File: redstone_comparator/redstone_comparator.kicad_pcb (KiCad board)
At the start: 2 copper layers, 40 x 40 mm, 77 parts, among them J1 1x4_Pogo, J2 1x4_Pogo, J3 1x4_Pogo, J4 1x4_Pogo, J5 1x4_Pogo, J6 1x4_Pogo, J7 1x4_Pogo, J8 1x4_Pogo, J9 2.54mm_ProgrammingPin, Q1 MMBT3904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

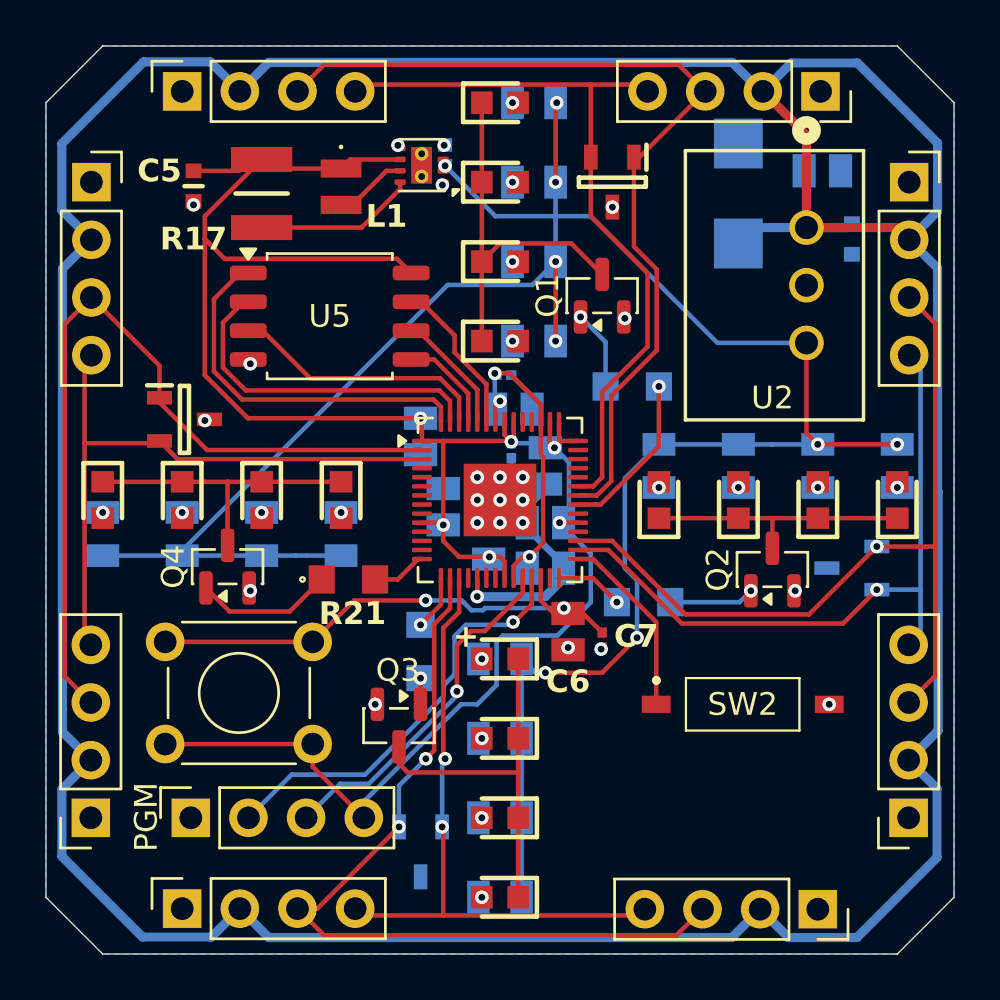
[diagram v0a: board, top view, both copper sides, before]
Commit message: finish routing all connections, todo align components and make it symmetric
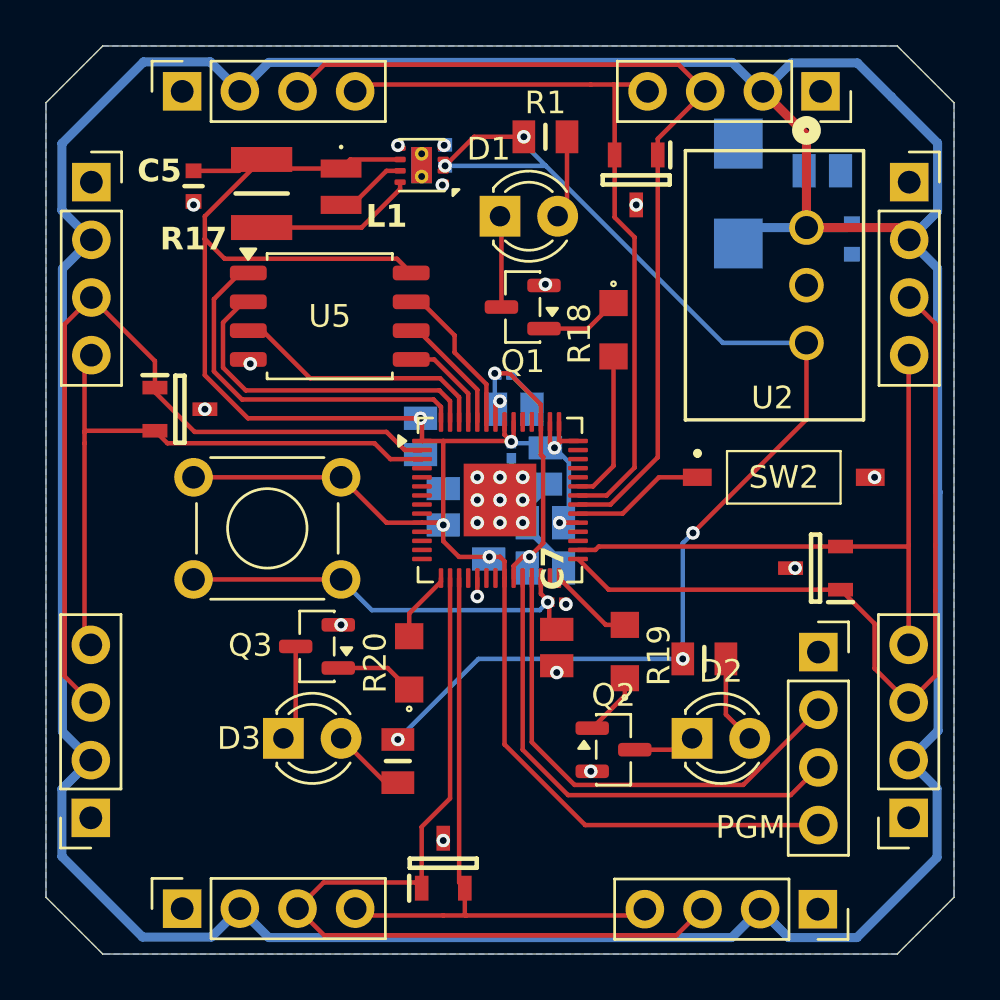
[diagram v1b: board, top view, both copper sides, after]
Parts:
- removed D10, D11, D12, D13, D14, D15, D16, D4, D5, D6, D7, D8, D9: LED, SamacSys_Parts:LEDC1608X115N
- removed Q4: MMBT3904, Package_TO_SOT_SMD:SOT-23
- removed R10, R11, R12, R13, R14, R15, R16, R4, R5, R6, R7, R8, R9: 200, SamacSys_Parts:CRCW1210200RJNEAIF
- removed R21: 1k, SamacSys_Parts:ERJ-UP6D1001V
- D1, D2, D3: footprint SamacSys_Parts:LEDC1608X115N -> LED_THT:LED_D3.0mm
- D18, D20, R1, R18, R19, R2, R20, R3: moved to F.Cu
- moved J9 28.6 mm to (149.0, 61.7), turned to 0 degrees
- moved D2 25.9 mm to (143.5, 65.5)
- moved D3 23.1 mm to (125.5, 65.5)
- moved R3 22.8 mm to (130.5, 66.5), turned to -90 degrees
- moved R2 22.3 mm to (144.0, 62.0), turned to 0 degrees
- moved SW1 12.9 mm to (121.5, 54.0), turned to 0 degrees
- moved Q2 10.6 mm to (140.0, 66.0), turned to 0 degrees
- moved SW2 10.2 mm to (147.5, 54.0)
- moved Q3 5.02 mm to (126.9, 61.5), turned to 180 degrees
- moved D1 5.00 mm to (135.0, 42.5)
- moved Q1 3.54 mm to (136.0, 46.5), turned to 180 degrees
- moved R18 2.63 mm to (140.0, 47.5), turned to -90 degrees
- moved C7 2.61 mm to (137.5, 59.5), turned to 0 degrees
- moved R19 2.33 mm to (140.5, 61.7), turned to 90 degrees
- moved D18 1.60 mm to (148.9, 58.0)
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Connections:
- D2 pad 1: Net-(D1-K) -> Net-(D2-K)
- D3 pad 1: Net-(D1-K) -> Net-(D3-K)
- Q2 pad 3: Net-(D5-K) -> Net-(D2-K)
- Q3 pad 3: Net-(D10-K) -> Net-(D3-K)
- R18 pad 2: Net-(U1-GPIO23) -> Net-(U1-GPIO25)
- SW2 pad 1: Net-(U1-GPIO18) -> Net-(U1-GPIO22)
- U1 pad 14: Net-(U1-GPIO11) -> unconnected-(U1-GPIO11-Pad14)
- U1 pad 29: Net-(U1-GPIO18) -> /E_TX
- U1 pad 31: /E_TX -> unconnected-(U1-GPIO20-Pad31)
- U1 pad 34: unconnected-(U1-GPIO22-Pad34) -> Net-(U1-GPIO22)
- U1 pad 35: Net-(U1-GPIO23) -> /N_TX
- U1 pad 36: /N_TX -> /N_RX
- U1 pad 37: /N_RX -> Net-(U1-GPIO25)
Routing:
- net /5V_LOCAL: track 103.9 -> 55.8 mm, vias 9 -> 5
- net Net-(D10-K): track 16.7 -> 0.00 mm
- net Net-(D13-K): track 13.3 -> 0.00 mm
- net Net-(D1-K): track 16.7 -> 3.94 mm
- net Net-(D5-K): track 11.8 -> 0.00 mm
- net Net-(U1-GPIO18): track 8.21 -> 0.00 mm
- net Net-(U1-GPIO23): track 7.26 -> 0.00 mm, vias 1 -> 0
- net Net-(U1-GPIO25): track 0.00 -> 6.76 mm
- net Net-(J9-Pin_3): track 15.6 -> 21.9 mm, vias 1 -> 0
- net Net-(Q4-B): track 6.12 -> 0.00 mm
- net Net-(U1-GPIO22): track 0.00 -> 5.92 mm
- net GND: track 15.4 -> 11.0 mm, vias 24 -> 25
- net Net-(D3-K): track 0.00 -> 4.27 mm
- net Net-(SW1-B): track 23.1 -> 18.9 mm, vias 2 -> 1
- net Net-(D2-A): track 0.25 -> 3.93 mm, vias 1 -> 0
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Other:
- board text removed: "+"

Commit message: generate gerber files for all blocks
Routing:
- net GND: track 11.0 -> 12.6 mm
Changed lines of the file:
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@@
 			(outputformat 1)
 			(mirror no)
-			(drillshape 1)
+			(drillshape 0)
 			(scaleselection 1)
-			(outputdirectory "")
+			(outputdirectory "../GERBERs/")
 		)
 	)
@@
 		(tags "LED")
 		(property "Reference" "D2"
-			(at 1.27 -2.96 0)
+			(at -0.46 2.5 0)
 			(layer "F.SilkS")
 			(effects
@@
 		(tags "SOT TO_SOT_SMD")
 		(property "Reference" "Q2"
-			(at 0 -2.4 0)
+			(at -2 -2 0)
 			(layer "F.SilkS")
 			(effects
@@
 		(tags "Capacitor")
 		(property "Reference" "C7"
-			(at -0.17 -1.5 90)
+			(at 1.5 0.5 90)
 			(layer "F.SilkS")
 			(effects
@@
 	)
 	(segment
+		(start 137.906985 59.593015)
+		(end 137.906985 58.106985)
+		(width 0.4)
+		(layer "B.Cu")
+		(net 2)
+	)
+	(segment
 		(start 136.41 51)
 		(end 136.41 50.41)
@@
 	)
 	(segment
+		(start 137.906985 58.106985)
+		(end 137.8 58)
+		(width 0.2)
+		(layer "B.Cu")
+		(net 2)
+	)
+	(segment
 		(start 136.41 50.41)
 		(end 135.5 49.5)
@@
 	)
 	(segment
-		(start 139.6625 60.5)
+		(start 137.9375 58.4375)
 		(end 137.6 58.4375)
 		(width 0.2)
@@
 	)
 	(segment
+		(start 140 60.5)
+		(end 137.9375 58.4375)
+		(width 0.2)
+		(layer "F.Cu")
+		(net 25)
+	)
+	(segment
 		(start 140.5 60.5)
-		(end 139.6625 60.5)
+		(end 140 60.5)
 		(width 0.2)
 		(layer "F.Cu")
